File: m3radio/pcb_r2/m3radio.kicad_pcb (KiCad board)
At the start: 2 copper layers, 39.5 x 39.5 mm, 65 parts, among them IC1 NCP380, IC101 STM32F405RxTx, IC102 MCP2562, IC2 NC7SZ04, IC201 Si4460, IC3 CS2100-CP, IC4 SL18860DC, IC5 MAX_M8Q, IC6 SN74LVC1G0832, J101 WEST TOP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

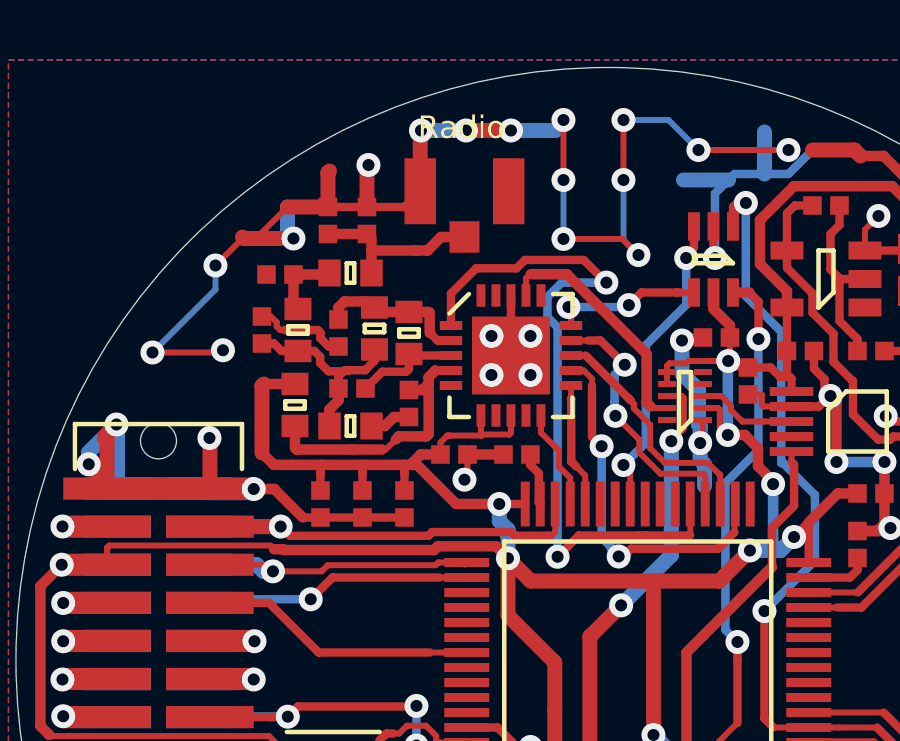
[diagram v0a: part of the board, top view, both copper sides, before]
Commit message: Add potential divider and small changes to radio pcb
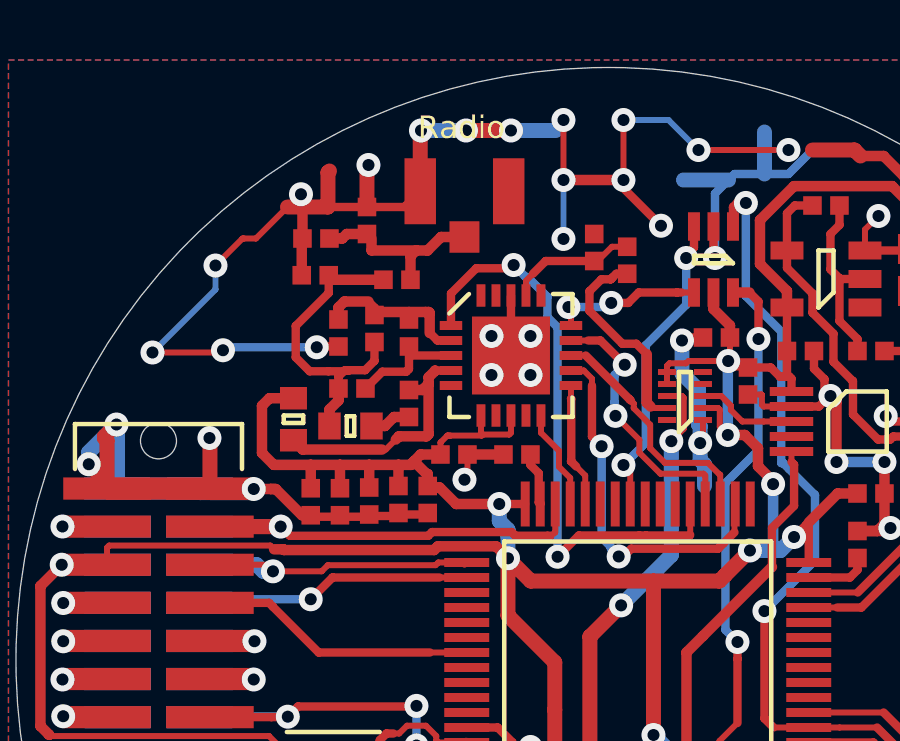
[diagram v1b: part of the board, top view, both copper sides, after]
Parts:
- removed C208: 4.7p, agg:0402
- removed L206: 6.8nH, agg:0603-L
- added C12: 220p, agg:0402, F.Cu at (93.0, 94.7)
- added C13: 2.2u, agg:0402, F.Cu at (90.1, 94.7)
- added R4: 10k, agg:0402, F.Cu at (100.6, 86.7)
- added R5: 10k, agg:0402, F.Cu at (99.5, 86.2)
- C103: value 4µ7 -> 4u7
- C110, C111: value 2µ2 -> 2u2
- C204: value 36p -> 22p
- C205: value 1.2p -> 1p
- C206: value 3.3p -> 5.6p
- C207: value 10p -> 5.6p
- IC201: value Si4460 -> Si4461
- L202: value 18nH -> 20nH; footprint agg:0603-L -> agg:0402
- L203: value 22nH -> 24nH; footprint agg:0603-L -> agg:0402
- L204: value 6.8nH -> 8.2nH
- L205: footprint agg:0603-L -> agg:0402
- moved C201 4.75 mm to (94.8, 93.2), turned to 0 degrees
- moved L205 3.70 mm to (93.0, 87.3), turned to 0 degrees
- moved C206 2.55 mm to (90.2, 87.2), turned to 180 degrees
- moved C109 1.74 mm to (94.0, 94.7), turned to 90 degrees
- moved C207 1.70 mm to (90.2, 86.0)
- moved C202 1.18 mm to (92.0, 94.7)
- moved C6 0.75 mm to (91.0, 94.7)
- moved L201 0.48 mm to (89.5, 92.0)
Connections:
- D2 pad 1: Net-(C208-Pad1) -> Net-(C207-Pad1)
- IC101 pad 10: Net-(IC101-Pad10) -> (no net)
- IC101 pad 11: Net-(IC101-Pad11) -> (no net)
- IC101 pad 2: Net-(IC101-Pad2) -> (no net)
- IC101 pad 23: Net-(IC101-Pad23) -> (no net)
- IC101 pad 24: Net-(IC101-Pad24) -> (no net)
- IC101 pad 25: Net-(IC101-Pad25) -> (no net)
- IC101 pad 26: Net-(IC101-Pad26) -> (no net)
- IC101 pad 27: Net-(IC101-Pad27) -> (no net)
- IC101 pad 28: Net-(IC101-Pad28) -> (no net)
- IC101 pad 33: Net-(IC101-Pad33) -> (no net)
- IC101 pad 38: Net-(IC101-Pad38) -> (no net)
- IC101 pad 39: Net-(IC101-Pad39) -> (no net)
- IC101 pad 40: Net-(IC101-Pad40) -> (no net)
- IC101 pad 42: Net-(IC101-Pad42) -> (no net)
- IC101 pad 43: Net-(IC101-Pad43) -> (no net)
- IC101 pad 51: Net-(IC101-Pad51) -> (no net)
- IC101 pad 52: Net-(IC101-Pad52) -> (no net)
- IC101 pad 53: Net-(IC101-Pad53) -> (no net)
- IC101 pad 54: Net-(IC101-Pad54) -> (no net)
- IC101 pad 56: Net-(IC101-Pad56) -> (no net)
- IC101 pad 57: Net-(IC101-Pad57) -> (no net)
- IC101 pad 58: Net-(IC101-Pad58) -> (no net)
- IC101 pad 59: Net-(IC101-Pad59) -> (no net)
- IC101 pad 6: Net-(IC101-Pad6) -> (no net)
- IC101 pad 7: Net-(IC101-Pad7) -> (no net)
- IC101 pad 8: Net-(IC101-Pad8) -> (no net)
- IC101 pad 9: Net-(IC101-Pad9) -> (no net)
- IC2 pad 1: Net-(IC2-Pad1) -> (no net)
- IC201 pad 16: Net-(IC201-Pad16) -> (no net)
- IC201 pad 17: /Radio_CLK -> Net-(IC201-Pad17)
- IC201 pad 19: Net-(IC201-Pad19) -> (no net)
- IC201 pad 20: Net-(IC201-Pad20) -> (no net)
- IC201 pad 5: Net-(IC201-Pad5) -> (no net)
- IC201 pad 7: Net-(IC201-Pad7) -> (no net)
- IC201 pad 9: Net-(IC201-Pad9) -> (no net)
- IC3 pad 4: Net-(IC3-Pad4) -> (no net)
- IC3 pad 6: Net-(IC3-Pad6) -> (no net)
- IC4 pad 10: Net-(IC4-Pad10) -> (no net)
- IC4 pad 4: Net-(IC4-Pad4) -> (no net)
- IC4 pad 5: Net-(IC4-Pad5) -> (no net)
- IC5 pad 13: Net-(IC5-Pad13) -> (no net)
- IC5 pad 15: Net-(IC5-Pad15) -> (no net)
- IC5 pad 16: Net-(IC5-Pad16) -> (no net)
- IC5 pad 17: Net-(IC5-Pad17) -> (no net)
- IC5 pad 5: Net-(IC5-Pad5) -> (no net)
- P201 pad 1: Net-(C208-Pad1) -> Net-(C207-Pad1)
- U1 pad 2: Net-(U1-Pad2) -> (no net)
- Y1 pad 1: Net-(Y1-Pad1) -> (no net)
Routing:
- net Net-(C208-Pad1): track 5.95 -> 0.00 mm
- net Net-(IC201-Pad17): track 0.00 -> 4.34 mm
- net /Radio_SDN: track 23.7 -> 19.7 mm
- net Net-(C207-Pad1): track 2.43 -> 6.26 mm
- net Net-(C205-Pad2): track 6.80 -> 10.4 mm
- net /Radio_CLK: track 8.11 -> 7.11 mm
- net /Radio/TX_pin: track 8.54 -> 7.96 mm
- net GND: track 326.6 -> 326.7 mm, vias 80 -> 81

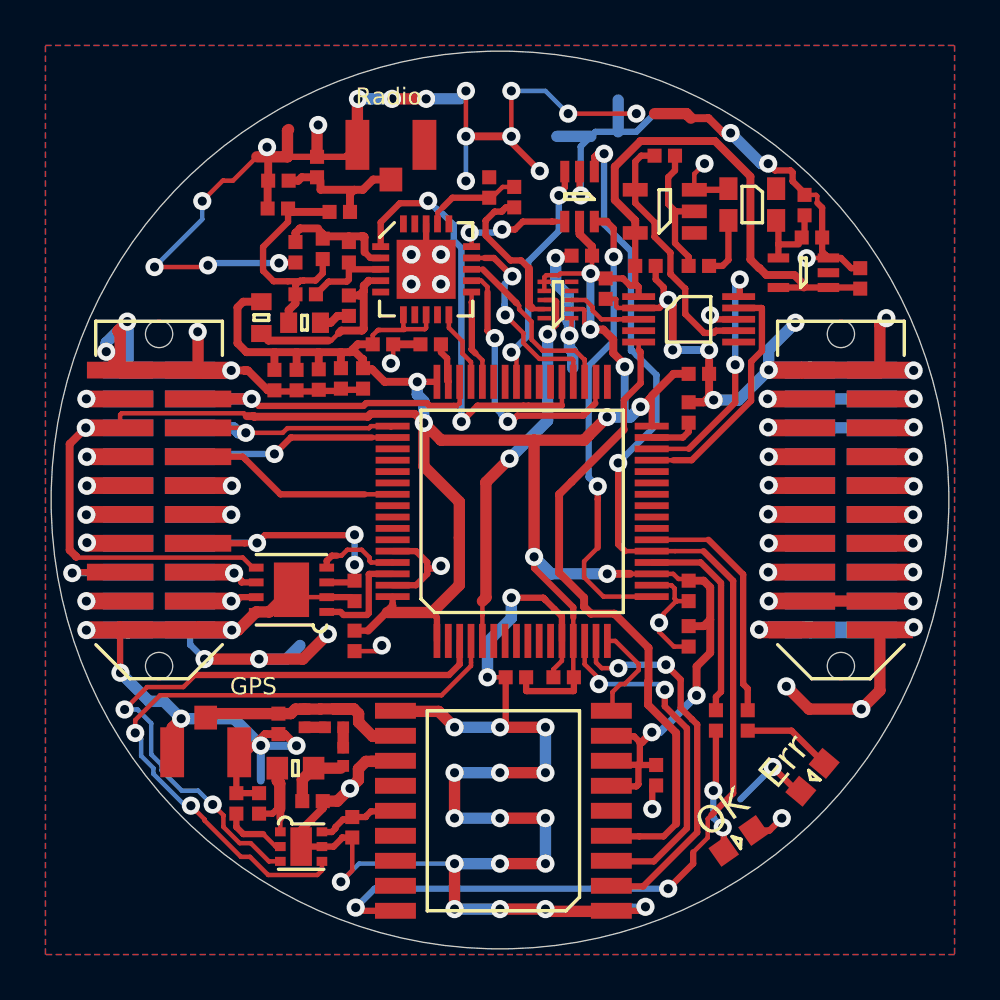
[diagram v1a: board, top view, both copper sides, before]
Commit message: Tidy up RF section and generate gerbers for manufacture.
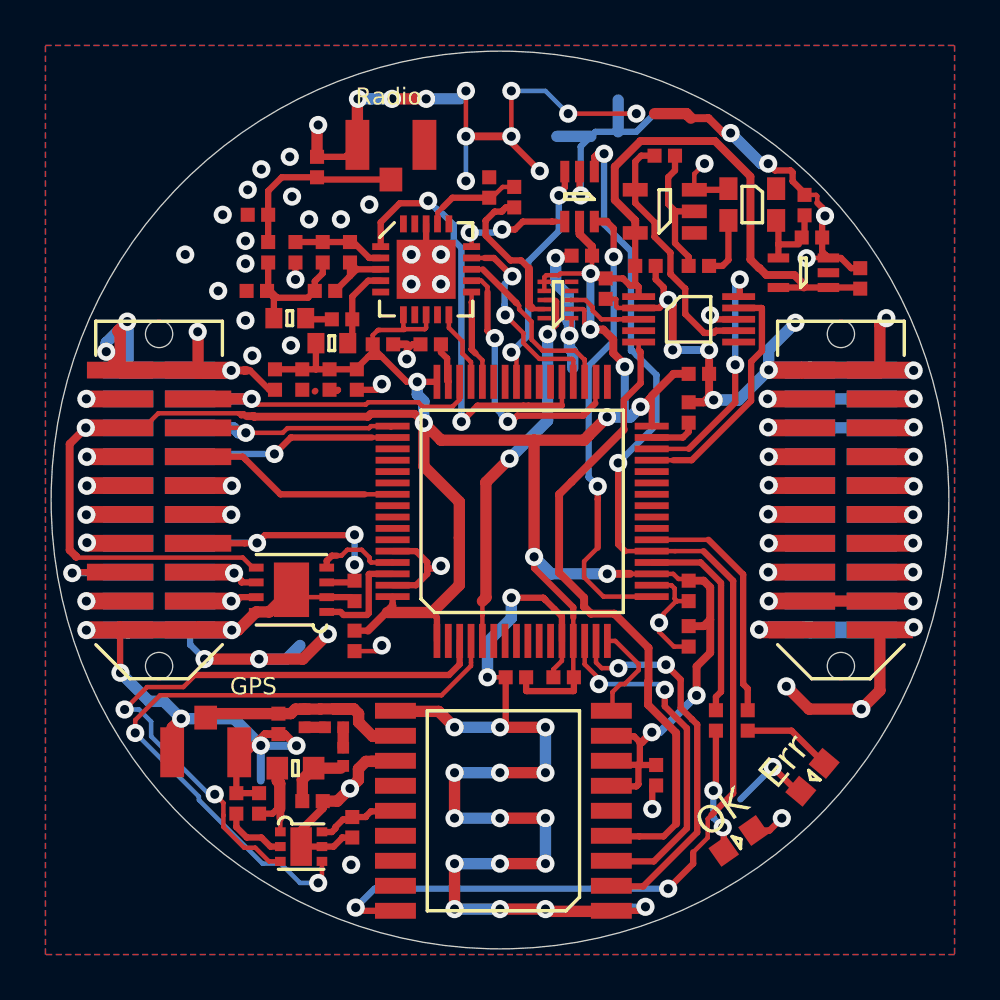
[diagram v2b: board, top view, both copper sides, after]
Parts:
- removed C6: 1u, agg:0402
- moved C206 3.74 mm to (89.3, 90.8)
- moved L205 3.62 mm to (89.8, 89.1), turned to 90 degrees
- moved L201 3.30 mm to (92.6, 93.1), turned to 0 degrees
- moved C207 1.75 mm to (89.3, 87.5)
- moved C205 0.86 mm to (92.3, 90.8)
- moved C202 0.73 mm to (91.3, 94.7)
- moved L204 0.68 mm to (90.8, 92.0)
- moved C204 0.67 mm to (93.0, 92.0), turned to 180 degrees
- moved C12 0.50 mm to (92.5, 94.7)
- moved C109 0.28 mm to (93.7, 94.7)
- moved L203 0.15 mm to (92.2, 89.1)
- moved L202 0.05 mm to (93.4, 89.1)
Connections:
- IC101 pad 10: (no net) -> Net-(IC101-Pad10)
- IC101 pad 11: (no net) -> Net-(IC101-Pad11)
- IC101 pad 2: (no net) -> Net-(IC101-Pad2)
- IC101 pad 23: (no net) -> Net-(IC101-Pad23)
- IC101 pad 24: (no net) -> Net-(IC101-Pad24)
- IC101 pad 25: (no net) -> Net-(IC101-Pad25)
- IC101 pad 26: (no net) -> Net-(IC101-Pad26)
- IC101 pad 27: (no net) -> Net-(IC101-Pad27)
- IC101 pad 28: (no net) -> Net-(IC101-Pad28)
- IC101 pad 33: (no net) -> Net-(IC101-Pad33)
- IC101 pad 38: (no net) -> Net-(IC101-Pad38)
- IC101 pad 39: (no net) -> Net-(IC101-Pad39)
- IC101 pad 40: (no net) -> Net-(IC101-Pad40)
- IC101 pad 42: (no net) -> Net-(IC101-Pad42)
- IC101 pad 43: (no net) -> Net-(IC101-Pad43)
- IC101 pad 51: (no net) -> Net-(IC101-Pad51)
- IC101 pad 52: (no net) -> Net-(IC101-Pad52)
- IC101 pad 53: (no net) -> Net-(IC101-Pad53)
- IC101 pad 54: (no net) -> Net-(IC101-Pad54)
- IC101 pad 56: (no net) -> Net-(IC101-Pad56)
- IC101 pad 57: (no net) -> Net-(IC101-Pad57)
- IC101 pad 58: (no net) -> Net-(IC101-Pad58)
- IC101 pad 59: (no net) -> Net-(IC101-Pad59)
- IC101 pad 6: (no net) -> Net-(IC101-Pad6)
- IC101 pad 7: (no net) -> Net-(IC101-Pad7)
- IC101 pad 8: (no net) -> Net-(IC101-Pad8)
- IC101 pad 9: (no net) -> Net-(IC101-Pad9)
- IC2 pad 1: (no net) -> Net-(IC2-Pad1)
- IC201 pad 16: (no net) -> Net-(IC201-Pad16)
- IC201 pad 19: (no net) -> Net-(IC201-Pad19)
- IC201 pad 20: (no net) -> Net-(IC201-Pad20)
- IC201 pad 5: (no net) -> Net-(IC201-Pad5)
- IC201 pad 7: (no net) -> Net-(IC201-Pad7)
- IC201 pad 9: (no net) -> Net-(IC201-Pad9)
- IC3 pad 4: (no net) -> Net-(IC3-Pad4)
- IC3 pad 6: (no net) -> Net-(IC3-Pad6)
- IC4 pad 10: (no net) -> Net-(IC4-Pad10)
- IC4 pad 4: (no net) -> Net-(IC4-Pad4)
- IC4 pad 5: (no net) -> Net-(IC4-Pad5)
- IC5 pad 13: (no net) -> Net-(IC5-Pad13)
- IC5 pad 15: (no net) -> Net-(IC5-Pad15)
- IC5 pad 16: (no net) -> Net-(IC5-Pad16)
- IC5 pad 17: (no net) -> Net-(IC5-Pad17)
- IC5 pad 5: (no net) -> Net-(IC5-Pad5)
- U1 pad 2: (no net) -> Net-(U1-Pad2)
- Y1 pad 1: (no net) -> Net-(Y1-Pad1)
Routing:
- net GND: track 326.7 -> 297.7 mm, vias 81 -> 94
- net 3v3: track 165.6 -> 159.4 mm
- net /Radio/TX_pin: track 7.96 -> 3.67 mm
- net Net-(C205-Pad2): track 10.4 -> 6.39 mm
- net Net-(C207-Pad1): track 6.26 -> 8.15 mm
- net /Radio/RXp: track 5.37 -> 4.25 mm
